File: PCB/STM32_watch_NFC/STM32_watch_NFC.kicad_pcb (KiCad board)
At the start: 4 copper layers, 40 x 40 mm, 107 parts, among them J1 Conn_01x06_Socket, J2 USB_C_Receptacle_PowerOnly_6P, Q1 2N7000, SW1 SW_DPST_x2, SW2 SW_DPST_x2, SW3 SW_DPST_x2, U1 STM32L031G6Ux, U2 MIC5365-3.3YC5, U3 ST25R3916-AQWT, U4 MT3608, Y1 27.12Mhz, Y2 32.768kHz

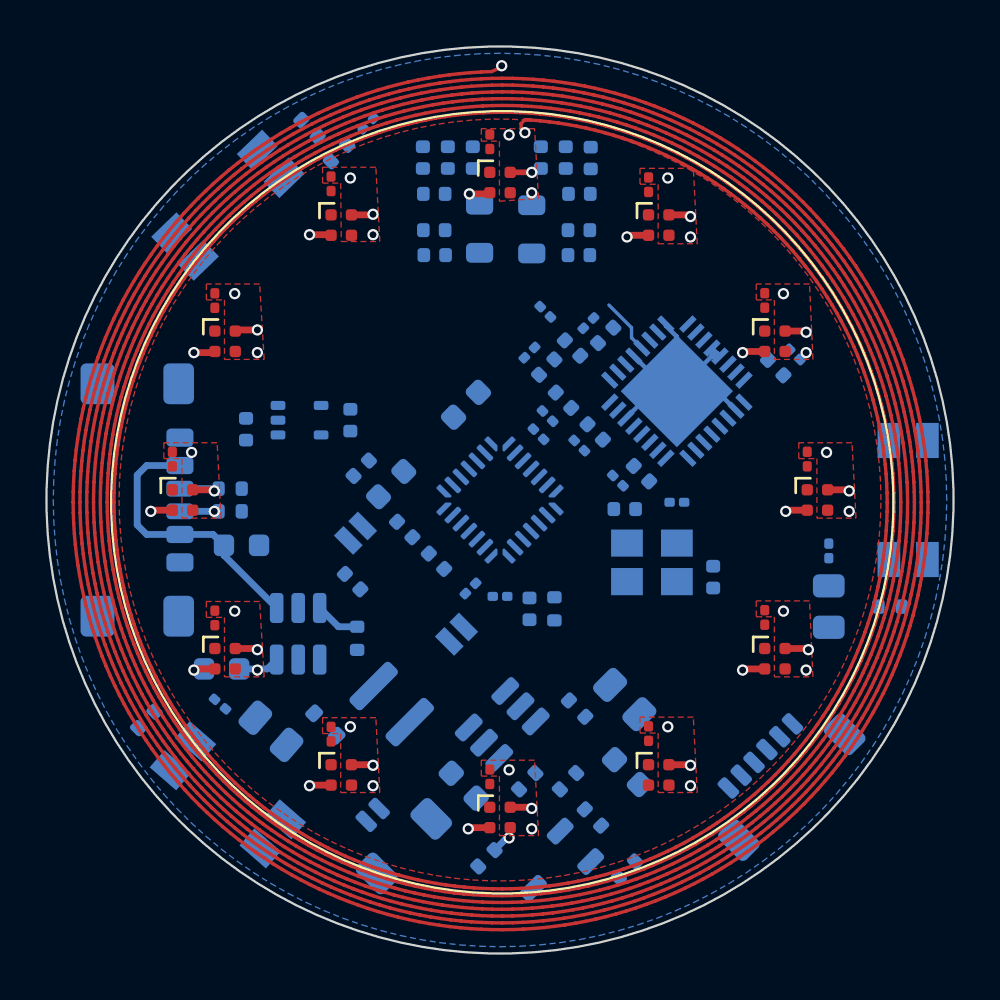
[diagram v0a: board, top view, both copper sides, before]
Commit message: Kicad - Routing 2
TOP and BOT layers have rough routing, I routed on IN 1 layer all RGB LEDs - so on TOP will not be any traces
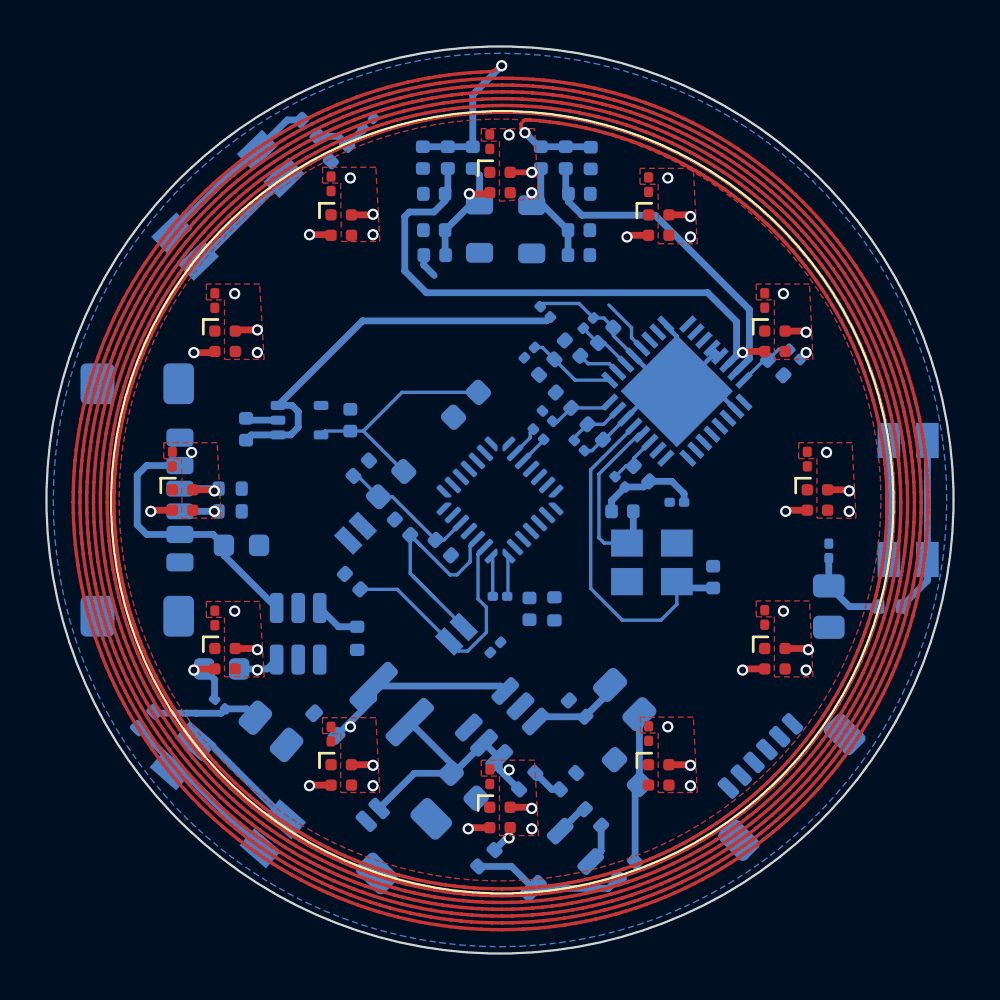
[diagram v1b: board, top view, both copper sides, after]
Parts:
- moved C49 4.94 mm to (153.9, 105.5), turned to 0 degrees
- moved C48 4.92 mm to (157.9, 108.4), turned to -90 degrees
- moved C7 2.82 mm to (148.3, 111.5)
- moved C3 0.67 mm to (146.0, 107.1)
- moved C9 0.14 mm to (144.2, 106.2)
- moved C34 0.11 mm to (153.8, 104.2)
- turned Y1 to 180 degrees
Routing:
- net /NFC_RFID/A1: track 0.00 -> 795.5 mm
- net unconnected-(U4-NC-Pad6): track 789.2 -> 0.00 mm
- net +3.3V: track 0.00 -> 31.1 mm
- net +5V: track 0.03 -> 29.3 mm
- net Net-(U3-RFI1): track 0.00 -> 23.5 mm
- net GND: track 15.0 -> 34.7 mm
- net Net-(U3-XTI): track 0.00 -> 15.8 mm
- net Net-(U3-RFI2): track 0.00 -> 14.5 mm
- net /LSE_OUT: track 0.00 -> 11.7 mm
- net +BATT: track 1.82 -> 13.4 mm
- net /LSE_IN: track 0.00 -> 11.1 mm
- net Net-(D13-A): track 0.00 -> 8.76 mm
- net Net-(U3-XTO): track 0.00 -> 8.28 mm
- net Net-(SW1A-A): track 0.00 -> 7.84 mm
- net Net-(SW2A-A): track 0.00 -> 7.80 mm
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
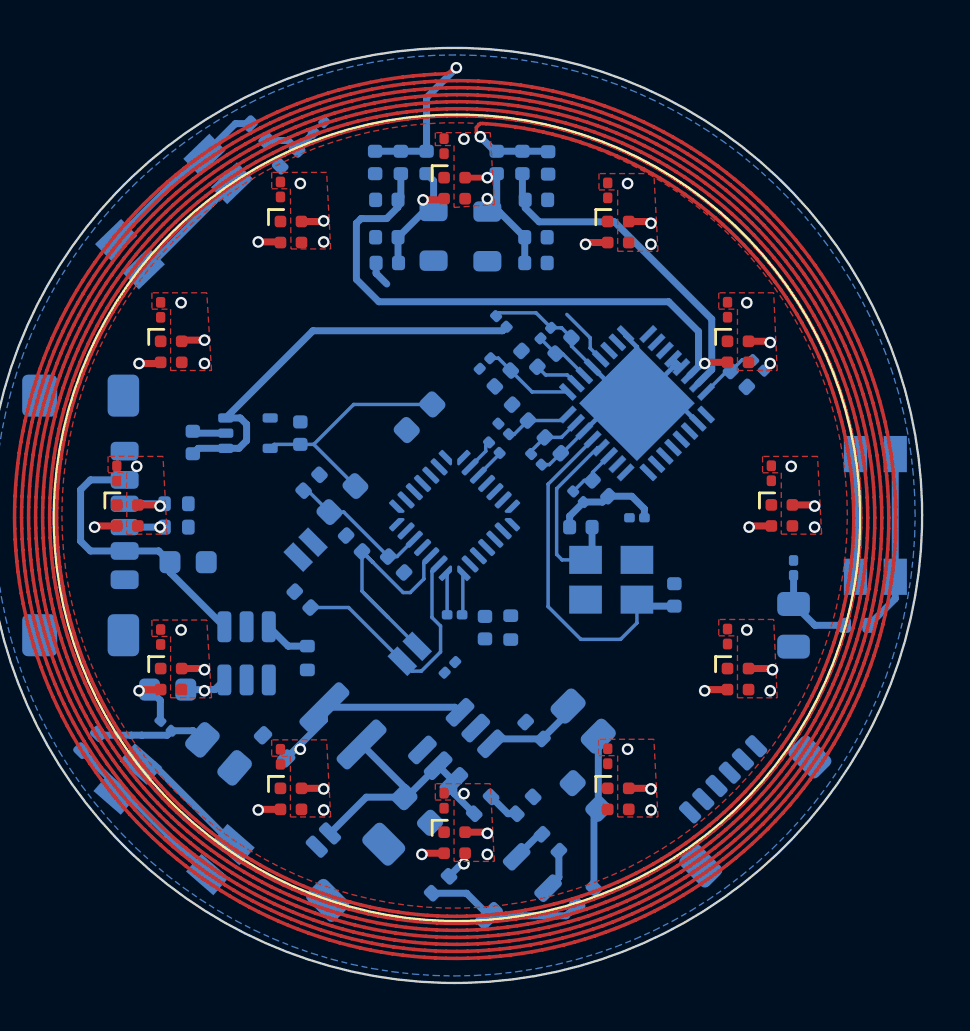
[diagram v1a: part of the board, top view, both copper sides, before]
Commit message: Kicad - Routing 3
Everything is routed BUT I found out I cant use blind/buried vias so... I need to redesign all vias :0
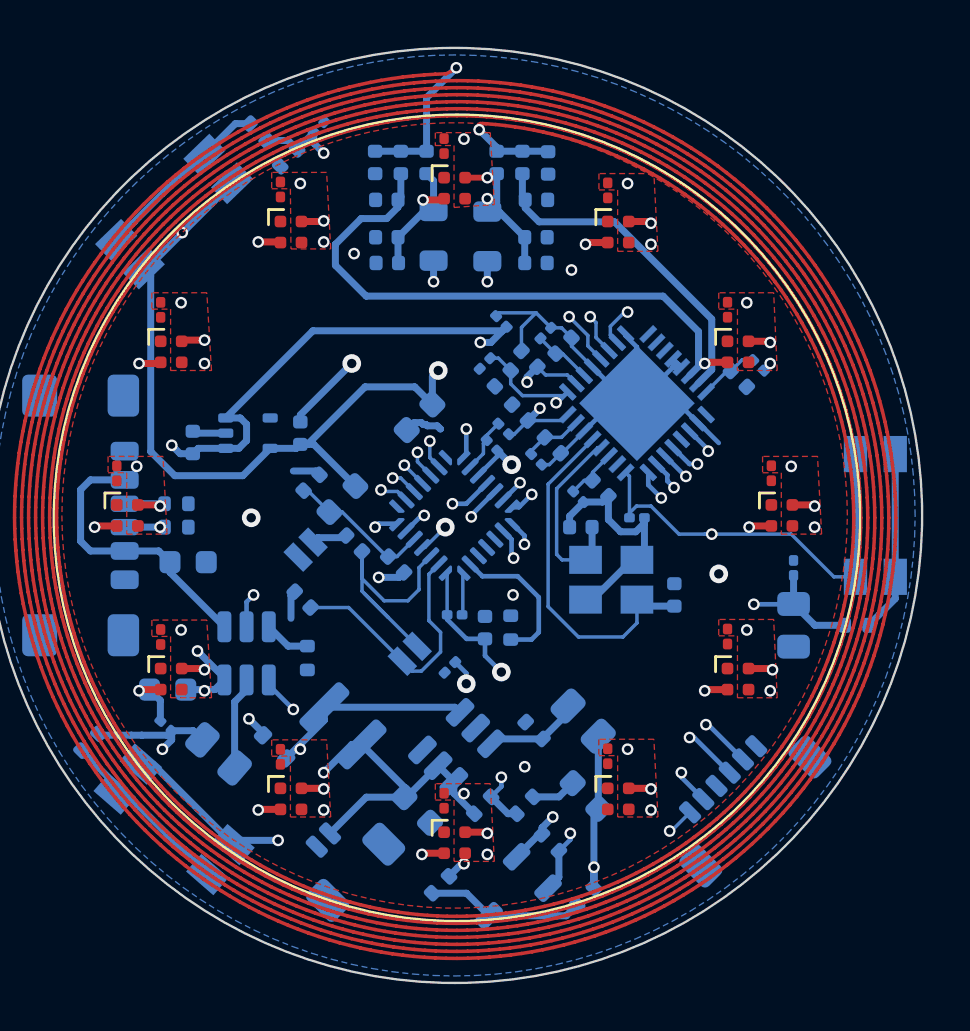
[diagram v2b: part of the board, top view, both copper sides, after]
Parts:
- moved C1 0.14 mm to (150.1, 102.0)
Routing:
- net GND: track 34.7 -> 221.1 mm, vias 24 -> 32
- net +3.3V: track 31.1 -> 147.8 mm, vias 0 -> 8
- net +5V: track 29.3 -> 75.1 mm, vias 0 -> 6
- net /NRST: track 0.00 -> 30.7 mm, vias 0 -> 3
- net Button_LT: track 2.47 -> 22.8 mm, vias 0 -> 2
- net SPI_IRQ_STM: track 0.00 -> 20.1 mm, vias 0 -> 2
- net SPI_CS_STM: track 0.00 -> 19.4 mm, vias 0 -> 2
- net /SWCLK: track 0.00 -> 19.1 mm, vias 0 -> 2
- net /SWDIO: track 0.00 -> 18.8 mm, vias 0 -> 2
- net Button_LB: track 4.72 -> 23.0 mm, vias 0 -> 2
- net BATT_STM: track 1.38 -> 19.4 mm, vias 0 -> 2
- net CHRG_STM: track 0.00 -> 17.7 mm, vias 0 -> 2
- net SPI_SCL_STM: track 0.00 -> 17.2 mm, vias 0 -> 2
- net DONE_STM: track 0.00 -> 17.2 mm, vias 0 -> 2
- net SPI_MISO_STM: track 0.00 -> 16.2 mm, vias 0 -> 2
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
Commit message: Kicad - Routing 4
Completed version. I just need to add graphics :)
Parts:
- added +BAT: 2.7-4.2V, TestPoint:TestPoint_Pad_D1.5mm, B.Cu at (145.1, 123.0)
- added 3V3: 3V3, TestPoint:TestPoint_Pad_D1.5mm, B.Cu at (138.8, 94.9)
- added 5V1: 5V, TestPoint:TestPoint_Pad_D1.5mm, B.Cu at (140.4, 96.9)
- added A1: ~, TestPoint:TestPoint_Pad_D1.5mm, B.Cu at (145.2, 87.3)
- added A2: ~, TestPoint:TestPoint_Pad_D1.5mm, B.Cu at (151.8, 87.3)
- added CLK: ~, TestPoint:TestPoint_Pad_D1.0mm, B.Cu at (156.7, 113.5)
- added D14: LED, LED_SMD:LED_0603_1608Metric, B.Cu at (162.3, 101.8)
- added DINS: ~, TestPoint:TestPoint_Pad_D1.0mm, B.Cu at (156.5, 120.3)
- added DIO: ~, TestPoint:TestPoint_Pad_D1.0mm, B.Cu at (157.9, 112.0)
- added D_BAT: ~, TestPoint:TestPoint_Pad_D1.0mm, B.Cu at (152.4, 110.9)
- added GND1: GND, TestPoint:TestPoint_Pad_D1.5mm, B.Cu at (160.4, 93.3)
- added JP1: SolderJumper_2_Open, Jumper:SolderJumper-2_P1.3mm_Open_TrianglePad1.0x1.5mm, B.Cu at (165.0, 99.6)
- added R18: 510, Resistor_SMD:R_0402_1005Metric, B.Cu at (160.2, 103.6)
- moved J1 1.45 mm to (159.8, 116.0)
- moved R13 1.40 mm to (134.1, 113.9)
- moved R11 1.31 mm to (141.1, 89.5), turned to 45 degrees
- moved R15 0.81 mm to (164.9, 109.6)
- moved R10 0.64 mm to (141.8, 90.2)
- moved C27 0.32 mm to (153.9, 116.8)
- moved Li-po1 0.27 mm to (143.6, 119.5)
- moved Q1 0.25 mm to (151.1, 121.0)
- moved C28 0.25 mm to (142.8, 88.6)
- moved R1 0.16 mm to (152.7, 118.8)
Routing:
- net GND: track 221.1 -> 231.5 mm
- net DIN_STM: track 15.5 -> 23.0 mm, vias 2 -> 4
- net +BATT: track 25.0 -> 32.1 mm
- net /SWCLK: track 19.1 -> 24.5 mm
- net +3.3V: track 147.8 -> 152.2 mm
- net BATT_STM: track 19.4 -> 22.4 mm, vias 2 -> 3
- net /SWDIO: track 18.8 -> 21.5 mm
- net Net-(D14-A): track 0.00 -> 2.64 mm
- net /NFC_RFID/A1: track 795.3 -> 797.8 mm
- net Net-(U4-FB): track 4.13 -> 6.40 mm
- net /NFC_RFID/A2: track 3.52 -> 5.78 mm
- net Net-(D14-K): track 0.00 -> 1.86 mm
- net +5V: track 75.1 -> 76.9 mm
- net Button_LB: track 23.0 -> 21.9 mm
- net Net-(SW3A-A): track 7.78 -> 8.78 mm
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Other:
- board text added: "HO HO"

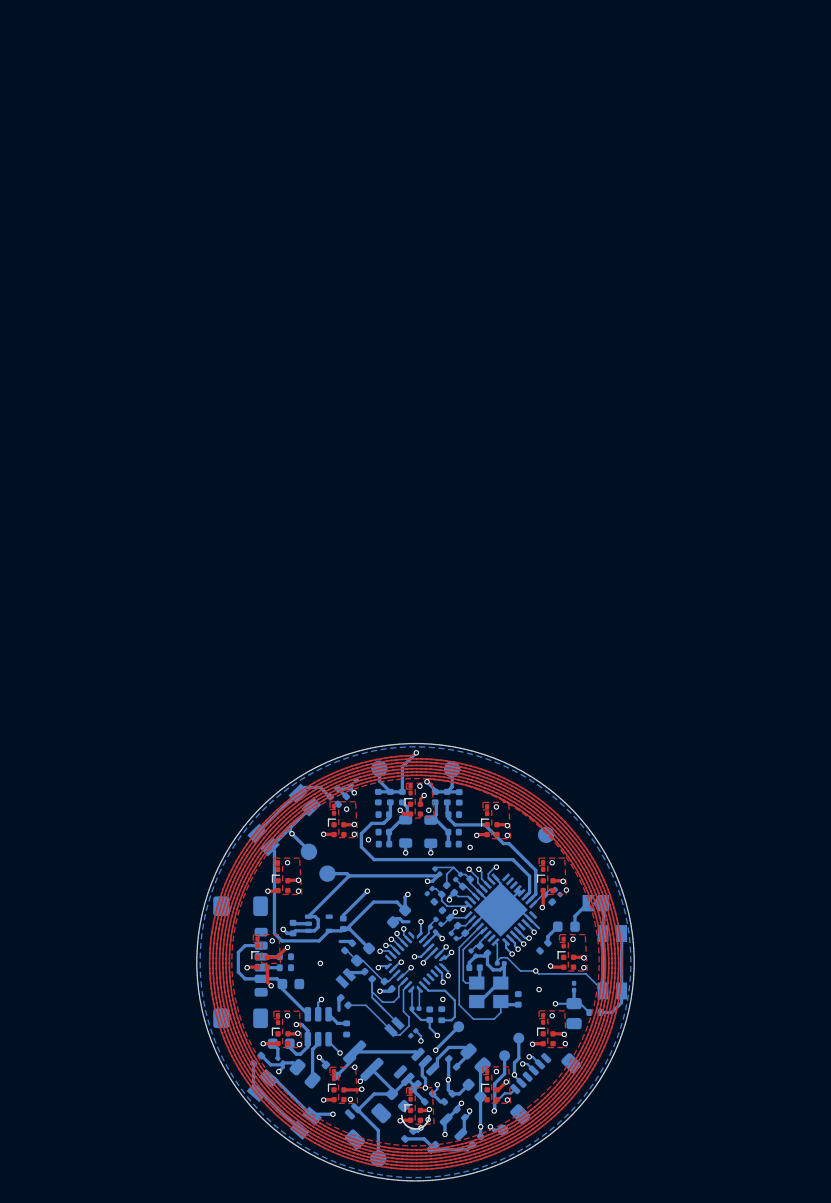
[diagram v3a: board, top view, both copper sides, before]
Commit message: Coding LEDs
Library for led management, buttons
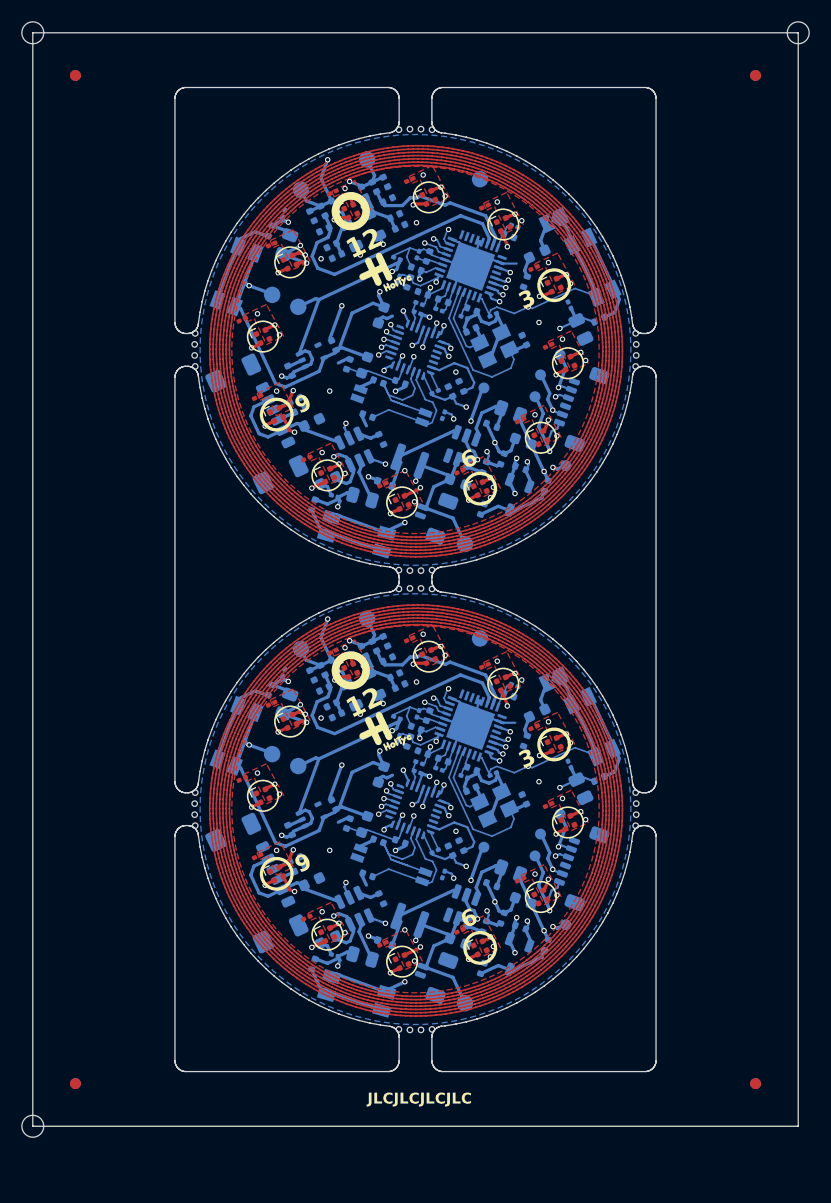
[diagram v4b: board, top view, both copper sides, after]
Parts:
- removed the +BAT at (145.1, 123.0)
- removed the 3V3 at (138.8, 94.9)
- removed 5V1: 5V, TestPoint:TestPoint_Pad_D1.5mm
- removed the A1 at (145.2, 87.3)
- removed the A2 at (151.8, 87.3)
- removed the CLK at (156.7, 113.5)
- removed the DINS at (156.5, 120.3)
- removed the DIO at (157.9, 112.0)
- removed the D_BAT at (152.4, 110.9)
- removed GND1: GND, TestPoint:TestPoint_Pad_D1.5mm
- removed the JP1 at (165.0, 99.6)
- added +BAT: 2.7-4.2V, TestPoint:TestPoint_Pad_D1.5mm, B.Cu at (153.0, 108.8)
- added +BAT: 2.7-4.2V, TestPoint:TestPoint_Pad_D1.5mm, B.Cu at (153.0, 66.8)
- added 3V3: 3V3, TestPoint:TestPoint_Pad_D1.5mm, B.Cu at (135.4, 44.0)
- added 3V3: 3V3, TestPoint:TestPoint_Pad_D1.5mm, B.Cu at (135.4, 86.0)
- added 5V: 5V, TestPoint:TestPoint_Pad_D1.5mm, B.Cu at (137.8, 87.1)
- added 5V: 5V, TestPoint:TestPoint_Pad_D1.5mm, B.Cu at (137.8, 45.1)
- added A1: ~, TestPoint:TestPoint_Pad_D1.5mm, B.Cu at (138.0, 34.4)
- added A1: ~, TestPoint:TestPoint_Pad_D1.5mm, B.Cu at (138.0, 76.4)
- added A2: ~, TestPoint:TestPoint_Pad_D1.5mm, B.Cu at (144.1, 31.6)
- added A2: ~, TestPoint:TestPoint_Pad_D1.5mm, B.Cu at (144.1, 73.6)
- added CLK: ~, TestPoint:TestPoint_Pad_D1.0mm, B.Cu at (159.4, 53.3)
- added CLK: ~, TestPoint:TestPoint_Pad_D1.0mm, B.Cu at (159.4, 95.3)
- added DINS: ~, TestPoint:TestPoint_Pad_D1.0mm, B.Cu at (162.3, 59.6)
- added DINS: ~, TestPoint:TestPoint_Pad_D1.0mm, B.Cu at (162.3, 101.6)
- added DIO: ~, TestPoint:TestPoint_Pad_D1.0mm, B.Cu at (159.9, 93.3)
- added DIO: ~, TestPoint:TestPoint_Pad_D1.0mm, B.Cu at (159.9, 51.3)
- added D_BAT: ~, TestPoint:TestPoint_Pad_D1.0mm, B.Cu at (154.8, 52.5)
- added D_BAT: ~, TestPoint:TestPoint_Pad_D1.0mm, B.Cu at (154.8, 94.5)
- added G***: LOGO, LOGO, F.Cu at (145.8, 41.9)
- added G***: LOGO, LOGO, F.Cu at (145.8, 83.9)
- added GND: GND, TestPoint:TestPoint_Pad_D1.5mm, B.Cu at (154.4, 33.4)
- added GND: GND, TestPoint:TestPoint_Pad_D1.5mm, B.Cu at (154.4, 75.4)
- added JP1: SolderJumper_2_Open, Jumper:SolderJumper-2_P1.3mm_Open_TrianglePad1.0x1.5mm, B.Cu at (161.2, 37.1)
- added JP1: SolderJumper_2_Open, Jumper:SolderJumper-2_P1.3mm_Open_TrianglePad1.0x1.5mm, B.Cu at (161.2, 79.1)
- added KiKit_FID_B_1: Fiducial, Fiducial, B.Cu at (117.4, 23.9)
- added KiKit_FID_B_2: Fiducial, Fiducial, B.Cu at (179.6, 23.9)
- added KiKit_FID_B_3: Fiducial, Fiducial, B.Cu at (117.4, 116.1)
- added KiKit_FID_B_4: Fiducial, Fiducial, B.Cu at (179.6, 116.1)
- added KiKit_FID_T_1: Fiducial, Fiducial, F.Cu at (117.4, 23.9)
- added KiKit_FID_T_2: Fiducial, Fiducial, F.Cu at (179.6, 23.9)
- added KiKit_FID_T_3: Fiducial, Fiducial, F.Cu at (117.4, 116.1)
- added KiKit_FID_T_4: Fiducial, Fiducial, F.Cu at (179.6, 116.1)
- added KiKit_MB_1_1: NPTH, NPTH, F.Cu at (128.4, 50.5)
- added KiKit_MB_1_2: NPTH, NPTH, F.Cu at (128.3, 49.5)
- added KiKit_MB_1_3: NPTH, NPTH, F.Cu at (128.3, 48.5)
- added KiKit_MB_1_4: NPTH, NPTH, F.Cu at (128.4, 47.5)
- added KiKit_MB_2_1: NPTH, NPTH, F.Cu at (168.6, 47.5)
- added KiKit_MB_2_2: NPTH, NPTH, F.Cu at (168.7, 48.5)
- added KiKit_MB_2_3: NPTH, NPTH, F.Cu at (168.7, 49.5)
- added KiKit_MB_2_4: NPTH, NPTH, F.Cu at (168.6, 50.5)
- added KiKit_MB_3_1: NPTH, NPTH, F.Cu at (147.0, 28.9)
- added KiKit_MB_3_2: NPTH, NPTH, F.Cu at (148.0, 28.8)
- added KiKit_MB_3_3: NPTH, NPTH, F.Cu at (149.0, 28.8)
- added KiKit_MB_3_4: NPTH, NPTH, F.Cu at (150.0, 28.9)
- added KiKit_MB_4_1: NPTH, NPTH, F.Cu at (150.0, 69.1)
- added KiKit_MB_4_2: NPTH, NPTH, F.Cu at (149.0, 69.2)
- added KiKit_MB_4_3: NPTH, NPTH, F.Cu at (148.0, 69.2)
- added KiKit_MB_4_4: NPTH, NPTH, F.Cu at (147.0, 69.1)
- added KiKit_MB_5_1: NPTH, NPTH, F.Cu at (128.4, 92.5)
- added KiKit_MB_5_2: NPTH, NPTH, F.Cu at (128.3, 91.5)
- added KiKit_MB_5_3: NPTH, NPTH, F.Cu at (128.3, 90.5)
- added KiKit_MB_5_4: NPTH, NPTH, F.Cu at (128.4, 89.5)
- added KiKit_MB_6_1: NPTH, NPTH, F.Cu at (168.6, 89.5)
- added KiKit_MB_6_2: NPTH, NPTH, F.Cu at (168.7, 90.5)
- added KiKit_MB_6_3: NPTH, NPTH, F.Cu at (168.7, 91.5)
- added KiKit_MB_6_4: NPTH, NPTH, F.Cu at (168.6, 92.5)
- added KiKit_MB_7_1: NPTH, NPTH, F.Cu at (147.0, 70.9)
- added KiKit_MB_7_2: NPTH, NPTH, F.Cu at (148.0, 70.8)
- added KiKit_MB_7_3: NPTH, NPTH, F.Cu at (149.0, 70.8)
- added KiKit_MB_7_4: NPTH, NPTH, F.Cu at (150.0, 70.9)
- added KiKit_MB_8_1: NPTH, NPTH, F.Cu at (150.0, 111.1)
- added KiKit_MB_8_2: NPTH, NPTH, F.Cu at (149.0, 111.2)
- added KiKit_MB_8_3: NPTH, NPTH, F.Cu at (148.0, 111.2)
- added KiKit_MB_8_4: NPTH, NPTH, F.Cu at (147.0, 111.1)
- added KiKit_TO_1: NPTH, NPTH, F.Cu at (113.5, 20.0)
- added KiKit_TO_2: NPTH, NPTH, F.Cu at (183.5, 20.0)
- added KiKit_TO_3: NPTH, NPTH, F.Cu at (113.5, 120.0)
- added NRST: ~, TestPoint:TestPoint_Pad_D1.0mm, B.Cu at (161.7, 91.5)
- added NRST: ~, TestPoint:TestPoint_Pad_D1.0mm, B.Cu at (161.7, 49.5)
- added TC1: 100n, Capacitor_SMD:C_0201_0603Metric, B.Cu at (148.7, 45.6)
- added TC10: 1u, Capacitor_SMD:C_0402_1005Metric, B.Cu at (137.0, 50.9)
- added TC11: 1u, Capacitor_SMD:C_0402_1005Metric, B.Cu at (141.0, 48.6)
- added TC12: 100n, Capacitor_SMD:C_0201_0603Metric, F.Cu at (140.9, 34.6)
- added TC13: 100n, Capacitor_SMD:C_0201_0603Metric, F.Cu at (148.0, 33.5)
- added TC14: 100n, Capacitor_SMD:C_0201_0603Metric, F.Cu at (154.9, 35.9)
- added TC15: 100n, Capacitor_SMD:C_0201_0603Metric, F.Cu at (159.3, 41.5)
- added TC16: 100n, Capacitor_SMD:C_0201_0603Metric, F.Cu at (160.7, 48.6)
- added TC17: 100n, Capacitor_SMD:C_0201_0603Metric, F.Cu at (158.1, 55.4)
- added TC18: 100n, Capacitor_SMD:C_0201_0603Metric, F.Cu at (152.6, 60.1)
- added TC19: 100n, Capacitor_SMD:C_0201_0603Metric, F.Cu at (145.5, 61.3)
- added TC2: 100n, Capacitor_SMD:C_0201_0603Metric, B.Cu at (150.3, 52.9)
- added TC20: 100n, Capacitor_SMD:C_0201_0603Metric, F.Cu at (138.6, 58.9)
- added TC21: 100n, Capacitor_SMD:C_0201_0603Metric, F.Cu at (134.1, 53.3)
- added TC22: 100n, Capacitor_SMD:C_0201_0603Metric, F.Cu at (132.7, 46.2)
- added TC23: 100n, Capacitor_SMD:C_0201_0603Metric, F.Cu at (135.3, 39.4)
- added TC24: 10u, Capacitor_SMD:C_0603_1608Metric, B.Cu at (139.0, 55.6)
- added TC25: 10u, Capacitor_SMD:C_0603_1608Metric, B.Cu at (140.5, 60.9)
- added TC26: 10u, Capacitor_SMD:C_0603_1608Metric, B.Cu at (152.4, 61.1)
- added TC27: 10u, Capacitor_SMD:C_0603_1608Metric, B.Cu at (158.4, 57.4)
- added TC28: 100n, Capacitor_SMD:C_0201_0603Metric, B.Cu at (136.4, 36.5)
- added TC29: 100n, Capacitor_SMD:C_0201_0603Metric, B.Cu at (141.1, 62.4)
- added TC3: 10n, Capacitor_SMD:C_0402_1005Metric, B.Cu at (147.1, 52.0)
- added TC30: 100n, Capacitor_SMD:C_0201_0603Metric, B.Cu at (162.6, 44.9)
- added TC31: 100n, Capacitor_SMD:C_0201_0603Metric, B.Cu at (155.6, 45.8)
- added TC34: 22n, Capacitor_SMD:C_0201_0603Metric, B.Cu at (153.0, 46.0)
- added TC35: 2.2uF, Capacitor_SMD:C_0402_1005Metric, B.Cu at (153.7, 45.3)
- added TC36: 22n, Capacitor_SMD:C_0201_0603Metric, B.Cu at (150.7, 45.3)
- added TC37: 2.2uF, Capacitor_SMD:C_0402_1005Metric, B.Cu at (151.0, 44.5)
- added TC38: 22n, Capacitor_SMD:C_0201_0603Metric, B.Cu at (148.7, 40.3)
- added TC39: 2.2uF, Capacitor_SMD:C_0402_1005Metric, B.Cu at (149.7, 40.5)
- added TC4: 10u, Capacitor_SMD:C_0603_1608Metric, B.Cu at (145.4, 45.8)
- added TC40: 22n, Capacitor_SMD:C_0201_0603Metric, B.Cu at (146.9, 42.6)
- added TC41: 2.2uF, Capacitor_SMD:C_0402_1005Metric, B.Cu at (147.9, 42.8)
- added TC42: 22n, Capacitor_SMD:C_0201_0603Metric, B.Cu at (146.8, 40.6)
- added TC43: 2.2uF, Capacitor_SMD:C_0402_1005Metric, B.Cu at (148.6, 41.6)
- added TC44: 22n, Capacitor_SMD:C_0201_0603Metric, B.Cu at (148.8, 44.8)
- added TC45: 2.2uF, Capacitor_SMD:C_0402_1005Metric, B.Cu at (149.2, 43.8)
- added TC46: 1u, Capacitor_SMD:C_0402_1005Metric, B.Cu at (157.1, 38.6)
- added TC47: 22n, Capacitor_SMD:C_0201_0603Metric, B.Cu at (157.6, 37.7)
- added TC48: 15pF, Capacitor_SMD:C_0402_1005Metric, B.Cu at (158.5, 48.1)
- added TC49: 15pF, Capacitor_SMD:C_0402_1005Metric, B.Cu at (153.6, 47.2)
- added TC5: 1u, Capacitor_SMD:C_0402_1005Metric, B.Cu at (142.4, 50.3)
- added TC50: 15pF, Capacitor_SMD:C_0402_1005Metric, B.Cu at (143.7, 34.6)
- added TC51: 15pF, Capacitor_SMD:C_0402_1005Metric, B.Cu at (141.0, 35.8)
- added TC52: 220pF, Capacitor_SMD:C_0402_1005Metric, B.Cu at (147.1, 37.7)
- added TC53: 220pF, Capacitor_SMD:C_0402_1005Metric, B.Cu at (140.8, 39.4)
- added TC54: 220pF, Capacitor_SMD:C_0402_1005Metric, B.Cu at (146.6, 36.7)
- added TC55: 220pF, Capacitor_SMD:C_0402_1005Metric, B.Cu at (141.3, 40.4)
- added TC56: 10pF, Capacitor_SMD:C_0402_1005Metric, B.Cu at (140.0, 36.3)
- added TC57: 220pF, Capacitor_SMD:C_0402_1005Metric, B.Cu at (140.2, 38.0)
- added TC58: 15pF, Capacitor_SMD:C_0402_1005Metric, B.Cu at (139.0, 36.8)
- added TC59: 15pF, Capacitor_SMD:C_0402_1005Metric, B.Cu at (145.7, 33.6)
- added TC6: 1u, Capacitor_SMD:C_0402_1005Metric, B.Cu at (151.7, 52.8)
- added TC60: 10pF, Capacitor_SMD:C_0402_1005Metric, B.Cu at (144.7, 34.1)
- added TC61: 220pF, Capacitor_SMD:C_0402_1005Metric, B.Cu at (146.0, 35.3)
- added TC7: 100n, Capacitor_SMD:C_0201_0603Metric, B.Cu at (151.1, 55.0)
- added TC8: 15pF, Capacitor_SMD:C_0402_1005Metric, B.Cu at (144.1, 55.0)
- added TC9: 15pF, Capacitor_SMD:C_0402_1005Metric, B.Cu at (145.1, 51.9)
- added TD1: SK6805, LED_SMD:LED_SK6812_EC15_1.5x1.5mm, F.Cu at (142.6, 36.3)
- added TD10: SK6805, LED_SMD:LED_SK6812_EC15_1.5x1.5mm, F.Cu at (135.8, 54.9)
- added TD11: SK6805, LED_SMD:LED_SK6812_EC15_1.5x1.5mm, F.Cu at (134.6, 47.8)
- added TD12: SK6805, LED_SMD:LED_SK6812_EC15_1.5x1.5mm, F.Cu at (137.0, 41.0)
- added TD13: D_Schottky, Diode_SMD:D_SOD-523, B.Cu at (145.7, 61.2)
- added TD14: LED, LED_SMD:LED_0603_1608Metric, B.Cu at (159.6, 40.2)
- added TD2: SK6805, LED_SMD:LED_SK6812_EC15_1.5x1.5mm, F.Cu at (149.7, 35.1)
- added TD3: SK6805, LED_SMD:LED_SK6812_EC15_1.5x1.5mm, F.Cu at (156.5, 37.5)
- added TD4: SK6805, LED_SMD:LED_SK6812_EC15_1.5x1.5mm, F.Cu at (161.2, 43.1)
- added TD5: SK6805, LED_SMD:LED_SK6812_EC15_1.5x1.5mm, F.Cu at (162.4, 50.2)
- added TD6: SK6805, LED_SMD:LED_SK6812_EC15_1.5x1.5mm, F.Cu at (160.0, 57.0)
- added TD7: SK6805, LED_SMD:LED_SK6812_EC15_1.5x1.5mm, F.Cu at (154.4, 61.7)
- added TD8: SK6805, LED_SMD:LED_SK6812_EC15_1.5x1.5mm, F.Cu at (147.3, 62.9)
- added TD9: SK6805, LED_SMD:LED_SK6812_EC15_1.5x1.5mm, F.Cu at (140.5, 60.5)
- added TFB1: FerriteBead, Inductor_SMD:L_0603_1608Metric, B.Cu at (143.9, 50.4)
- added TJ1: Conn_01x06_Socket, Connector_JST:JST_SUR_SM06B-SURS-TF_1x06-1MP_P0.80mm_Horizontal, B.Cu at (163.4, 54.2)
- added TJ2: USB_C_Receptacle_PowerOnly_6P, Connector_USB:USB_C_Receptacle_GCT_USB4135-GF-A_6P_TopMnt_Horizontal, B.Cu at (133.0, 56.2)
- added TL1: 22uH, Components:SLW3015, B.Cu at (148.0, 59.2)
- added TL2: 270nH 500mOhm, Inductor_SMD:L_0805_2012Metric, B.Cu at (144.7, 37.6)
- added TL3: 270nH 500mOhm, Inductor_SMD:L_0805_2012Metric, B.Cu at (142.6, 38.5)
- added TLi-po1: Conn_01x02_Socket, Connector_JST:JST_SUR_SM02B-SURS-TF_1x02-1MP_P0.80mm_Horizontal, B.Cu at (150.2, 64.2)
- added TME4055A1: ~, Package_TO_SOT_SMD:SOT-23-6, B.Cu at (142.9, 58.1)
- added TQ1: 2N7000, Package_TO_SOT_SMD:TSOT-23, B.Cu at (157.6, 62.4)
- added TR1: 10K, Resistor_SMD:R_0402_1005Metric, B.Cu at (158.1, 59.8)
- added TR10: 16.5K, Resistor_SMD:R_0805_2012Metric, B.Cu at (136.7, 39.4)
- added TR11: 510, Resistor_SMD:R_0402_1005Metric, B.Cu at (135.2, 38.1)
- added TR12: 16.5K, Resistor_SMD:R_0805_2012Metric, B.Cu at (143.7, 62.5)
- added TR13: 510, Resistor_SMD:R_0402_1005Metric, B.Cu at (139.2, 63.2)
- added TR14: 16.5K, Resistor_SMD:R_0805_2012Metric, B.Cu at (163.6, 47.1)
- added TR15: 510, Resistor_SMD:R_0402_1005Metric, B.Cu at (165.3, 46.2)
- added TR16: 10K, Resistor_SMD:R_0402_1005Metric, B.Cu at (154.8, 59.7)
- added TR17: 10K, Resistor_SMD:R_0402_1005Metric, B.Cu at (156.5, 59.0)
- added TR18: 510, Resistor_SMD:R_0402_1005Metric, B.Cu at (158.6, 42.8)
- added TR2: 10K, Resistor_SMD:R_0402_1005Metric, B.Cu at (160.5, 61.4)
- added TR3: 10K, Resistor_SMD:R_0402_1005Metric, B.Cu at (152.7, 52.3)
- added TR4: 5K1, Resistor_SMD:R_0402_1005Metric, B.Cu at (137.9, 54.5)
- added TR5: 5K1, Resistor_SMD:R_0402_1005Metric, B.Cu at (137.5, 53.6)
- added TR6: 510, Resistor_SMD:R_0402_1005Metric, B.Cu at (154.6, 63.6)
- added TR7: 5K1, Resistor_SMD:R_0402_1005Metric, B.Cu at (145.4, 57.2)
- added TR8: 16.5K, Resistor_SMD:R_0805_2012Metric, B.Cu at (157.2, 54.7)
- added TR9: 2.2K, Resistor_SMD:R_0402_1005Metric, B.Cu at (155.5, 55.9)
- added TSW1: SW_DPST_x2, Button_Switch_SMD:Panasonic_EVQPUJ_EVQPUA, B.Cu at (143.1, 65.9)
- added TSW2: SW_DPST_x2, Button_Switch_SMD:Panasonic_EVQPUJ_EVQPUA, B.Cu at (164.7, 41.5)
- added TSW3: SW_DPST_x2, Button_Switch_SMD:Panasonic_EVQPUJ_EVQPUA, B.Cu at (132.1, 42.3)
- added TU1: STM32L031G6Ux, Package_DFN_QFN:QFN-28_4x4mm_P0.5mm, B.Cu at (148.5, 49.0)
- added TU2: MIC5365-3.3YC5, Package_TO_SOT_SMD:SOT-353_SC-70-5, B.Cu at (139.0, 49.5)
- added TU3: ST25R3916-AQWT, ST25R3916-AQWT:QFN50P500X500X100-33N, B.Cu at (153.5, 41.4)
- added TU4: MT3608, Package_TO_SOT_SMD:SOT-23-6, B.Cu at (152.8, 57.9)
- added TY1: 27.12Mhz, Crystal:Crystal_SMD_3225-4Pin_3.2x2.5mm, B.Cu at (155.7, 48.7)
- added TY2: 32.768kHz, Crystal:Crystal_SMD_SeikoEpson_MC146-4Pin_6.7x1.5mm, B.Cu at (146.3, 54.1)
- R10: footprint Resistor_SMD:R_0402_1005Metric -> Resistor_SMD:R_0805_2012Metric
- R13: value 500 -> 510
- moved SW2 21.6 mm to (164.6, 83.5), turned to 115 degrees
- moved R15 21.4 mm to (165.3, 88.2), turned to -155 degrees
- moved R14 20.6 mm to (163.6, 89.1), turned to -65 degrees
- moved C30 20.3 mm to (162.6, 86.9), turned to -65 degrees
- moved J1 20.1 mm to (163.4, 96.2), turned to -110 degrees
- moved D4 20.0 mm to (161.2, 85.1), turned to 25 degrees
- moved C15 19.9 mm to (159.3, 83.5), turned to 25 degrees
- moved D5 19.9 mm to (162.4, 92.2), turned to 25 degrees
- moved D14 19.7 mm to (159.6, 82.2), turned to 25 degrees
- moved C16 19.6 mm to (160.7, 90.6), turned to 25 degrees
- moved C47 19.3 mm to (157.6, 79.7), turned to -20 degrees
- moved C14 19.1 mm to (154.9, 77.9), turned to 25 degrees
- moved R2 19.0 mm to (160.5, 103.4), turned to -110 degrees
- moved C46 18.9 mm to (157.1, 80.6), turned to 160 degrees
- moved D3 18.9 mm to (156.5, 79.5), turned to 25 degrees
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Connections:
- net +3.3V renamed Board_1-+3.3V
- net +3.3VA renamed Board_1-+3.3VA
- net +5V renamed Board_1-+5V
- net +BATT renamed Board_1-+BATT
- net /LSE_IN renamed Board_1-/LSE_IN
- net /LSE_OUT renamed Board_1-/LSE_OUT
- net /NFC_RFID/A1 renamed Board_1-/NFC_RFID/A1
- net /NFC_RFID/A2 renamed Board_1-/NFC_RFID/A2
- net /NRST renamed Board_1-/NRST
- net /SWCLK renamed Board_1-/SWCLK
- net /SWDIO renamed Board_1-/SWDIO
- net BATT_STM renamed Board_1-BATT_STM
- net Button_LB renamed Board_1-Button_LB
- net Button_LT renamed Board_1-Button_LT
- net Button_R renamed Board_1-Button_R
- net CHRG_STM renamed Board_1-CHRG_STM
- net DIN_LED renamed Board_1-DIN_LED
- net DIN_STM renamed Board_1-DIN_STM
- net DONE_STM renamed Board_1-DONE_STM
- net GND renamed Board_1-GND
- net Net-(C50-Pad1) renamed Board_1-Net-(C50-Pad1)
- net Net-(C51-Pad1) renamed Board_1-Net-(C51-Pad1)
- net Net-(D1-DIN) renamed Board_1-Net-(D1-DIN)
- net Net-(D1-DOUT) renamed Board_1-Net-(D1-DOUT)
- net Net-(D10-DIN) renamed Board_1-Net-(D10-DIN)
- net Net-(D10-DOUT) renamed Board_1-Net-(D10-DOUT)
- net Net-(D11-DOUT) renamed Board_1-Net-(D11-DOUT)
- net Net-(D13-A) renamed Board_1-Net-(D13-A)
- net Net-(D14-K) renamed Board_1-Net-(D14-K)
- net Net-(D2-DOUT) renamed Board_1-Net-(D2-DOUT)
- net Net-(D3-DOUT) renamed Board_1-Net-(D3-DOUT)
- net Net-(D4-DOUT) renamed Board_1-Net-(D4-DOUT)
- net Net-(D5-DOUT) renamed Board_1-Net-(D5-DOUT)
- net Net-(D7-DIN) renamed Board_1-Net-(D7-DIN)
- net Net-(D7-DOUT) renamed Board_1-Net-(D7-DOUT)
- net Net-(D8-DOUT) renamed Board_1-Net-(D8-DOUT)
- net Net-(J2-CC1) renamed Board_1-Net-(J2-CC1)
- net Net-(J2-CC2) renamed Board_1-Net-(J2-CC2)
- net Net-(ME4055A1-PROG) renamed Board_1-Net-(ME4055A1-PROG)
- net Net-(SW1A-A) renamed Board_1-Net-(SW1A-A)
- net Net-(SW2A-A) renamed Board_1-Net-(SW2A-A)
- net Net-(SW3A-A) renamed Board_1-Net-(SW3A-A)
- net Net-(U1-BOOT0) renamed Board_1-Net-(U1-BOOT0)
- net Net-(U3-AGDC) renamed Board_1-Net-(U3-AGDC)
- net Net-(U3-RFI1) renamed Board_1-Net-(U3-RFI1)
- net Net-(U3-RFI2) renamed Board_1-Net-(U3-RFI2)
- net Net-(U3-RFO1) renamed Board_1-Net-(U3-RFO1)
- net Net-(U3-RFO2) renamed Board_1-Net-(U3-RFO2)
- net Net-(U3-VDD_A) renamed Board_1-Net-(U3-VDD_A)
- net Net-(U3-VDD_AM) renamed Board_1-Net-(U3-VDD_AM)
- net Net-(U3-VDD_D) renamed Board_1-Net-(U3-VDD_D)
- net Net-(U3-VDD_DR) renamed Board_1-Net-(U3-VDD_DR)
- net Net-(U3-XTI) renamed Board_1-Net-(U3-XTI)
- net Net-(U3-XTO) renamed Board_1-Net-(U3-XTO)
- net Net-(U4-FB) renamed Board_1-Net-(U4-FB)
- net SPI_CS_STM renamed Board_1-SPI_CS_STM
- net SPI_IRQ_STM renamed Board_1-SPI_IRQ_STM
- net SPI_MISO_STM renamed Board_1-SPI_MISO_STM
- net SPI_MOSI_STM renamed Board_1-SPI_MOSI_STM
- net SPI_SCL_STM renamed Board_1-SPI_SCL_STM
- net VBUS renamed Board_1-VBUS
- D14 pad 2: Net-(D14-A) -> Board_1-Net-(D14-A)
- D6 pad 1: unconnected-(D6-DOUT-Pad1) -> Board_1-unconnected-(D6-DOUT-Pad1)
- J1 pad 1: unconnected-(J1-Pin_1-Pad1) -> Board_1-unconnected-(J1-Pin_1-Pad1)
- U1 pad 14: unconnected-(U1-PB0-Pad14) -> Board_1-unconnected-(U1-PB0-Pad14)
- U1 pad 24: unconnected-(U1-PB3-Pad24) -> Board_1-unconnected-(U1-PB3-Pad24)
- U1 pad 25: unconnected-(U1-PB6-Pad25) -> Board_1-unconnected-(U1-PB6-Pad25)
- U1 pad 26: unconnected-(U1-PB7-Pad26) -> Board_1-unconnected-(U1-PB7-Pad26)
- U1 pad 8: unconnected-(U1-PA2-Pad8) -> Board_1-unconnected-(U1-PA2-Pad8)
- U2 pad 4: unconnected-(U2-NC-Pad4) -> Board_1-unconnected-(U2-NC-Pad4)
- U3 pad 17: unconnected-(U3-EXT_LM-Pad17) -> Board_1-unconnected-(U3-EXT_LM-Pad17)
- U3 pad 18: unconnected-(U3-AAT_A-Pad18) -> Board_1-unconnected-(U3-AAT_A-Pad18)
- U3 pad 19: unconnected-(U3-AAT_B-Pad19) -> Board_1-unconnected-(U3-AAT_B-Pad19)
- U3 pad 2: unconnected-(U3-CSO-Pad2) -> Board_1-unconnected-(U3-CSO-Pad2)
- U3 pad 25: unconnected-(U3-CSI-Pad25) -> Board_1-unconnected-(U3-CSI-Pad25)
- U3 pad 28: unconnected-(U3-MCU_CLK-Pad28) -> Board_1-unconnected-(U3-MCU_CLK-Pad28)
- U4 pad 6: unconnected-(U4-NC-Pad6) -> Board_1-unconnected-(U4-NC-Pad6)
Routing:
- net Board_0-/NFC_RFID/A1: track 0.00 -> 797.8 mm, vias 0 -> 1
- net Board_0-GND: track 0.00 -> 237.5 mm, vias 0 -> 32
- net Board_0-+3.3V: track 0.00 -> 152.2 mm, vias 0 -> 8
- net Board_0-+5V: track 0.00 -> 76.9 mm, vias 0 -> 6
- net Board_0-/NRST: track 0.00 -> 33.8 mm, vias 0 -> 3
- net Board_0-+BATT: track 0.00 -> 32.1 mm, vias 0 -> 2
- net Board_0-/SWCLK: track 0.00 -> 24.5 mm, vias 0 -> 2
- net Board_0-Net-(U3-RFI1): track 0.00 -> 24.3 mm
- net Board_0-Button_LT: track 0.00 -> 24.3 mm, vias 0 -> 2
- net Board_0-DIN_STM: track 0.00 -> 23.0 mm, vias 0 -> 4
- net Board_0-BATT_STM: track 0.00 -> 22.4 mm, vias 0 -> 3
- net Board_0-Button_LB: track 0.00 -> 21.9 mm, vias 0 -> 2
- net Board_0-/SWDIO: track 0.00 -> 21.5 mm, vias 0 -> 2
- net Board_0-SPI_IRQ_STM: track 0.00 -> 20.2 mm, vias 0 -> 2
- net Board_0-SPI_CS_STM: track 0.00 -> 19.5 mm, vias 0 -> 2
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- added copper zone on F.Cu, net Board_0-+5V
- added copper zone on B.Cu, net Board_0-GND
- added copper zone on F.Cu, net Board_0-GND
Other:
- board size 40 x 40 mm -> 70 x 100 mm
- board text added: "+"
- board text added: "12"
- board text added: "3"
- board text added: "6"
- board text added: "9"
- board text added: "JLCJLCJLCJLC"
- board text added: "Rev.A.0"
